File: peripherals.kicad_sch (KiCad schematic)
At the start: 50 parts, among them J5 Out_to_display, U1 Boost Converter - TPS61169DCKR, U3 RA8875L3N, U7 74HC4050D, Y1 20MHz

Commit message: Some fixes
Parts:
- removed C25, C26: 0.1uF, Capacitor_SMD:C_0805_2012Metric, symbol Device:C
- removed C27: 1uF, Capacitor_SMD:C_0805_2012Metric, symbol Device:C
- C31: value 0.1uF -> 1uF
- R38: value R -> 10k
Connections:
- net +3.3V: no longer C30.1, C31.1, C34.1
- net GND: now also C30.1; no longer C30.2
- net +1V5 renamed CORE_VDD
- net CORE_VDD: now also C30.2, C31.1; no longer U3.5 (OSC_VDD)
- new net: C34.1, U3.5 (OSC_VDD)
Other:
- moved on the sheet: C23, C24, C28, C29, C30, C31, C33, C34

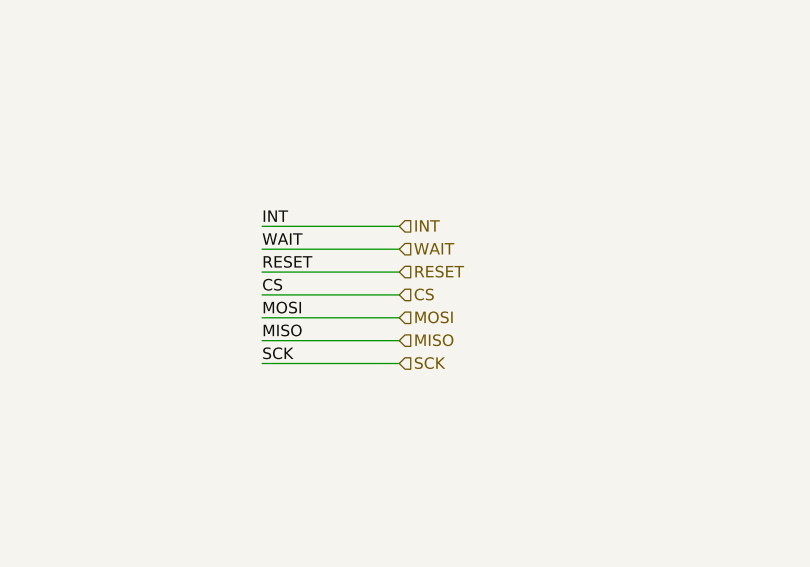
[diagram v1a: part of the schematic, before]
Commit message: Fixed labels and added datasheets
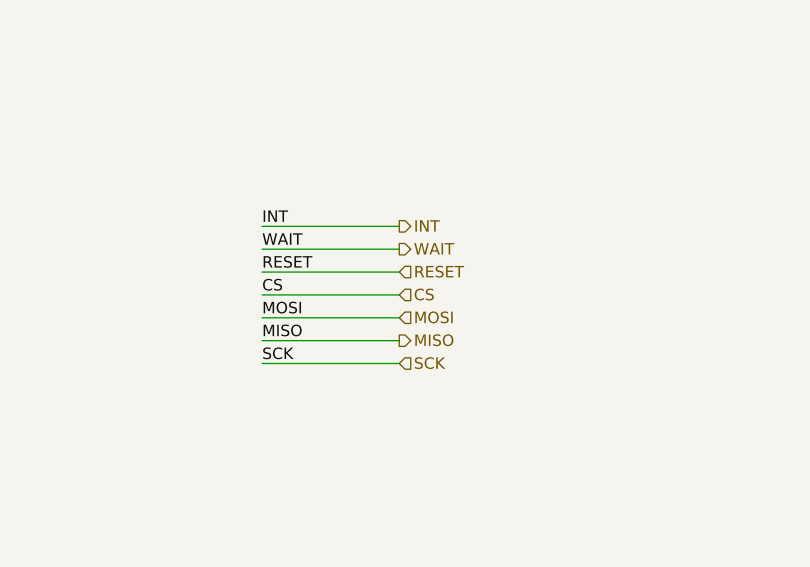
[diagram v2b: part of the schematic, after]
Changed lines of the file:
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@@
 	)
 	(hierarchical_label "INT"
-		(shape input)
+		(shape output)
 		(at 247.65 111.76 0)
 		(effects
@@
 	)
 	(hierarchical_label "MISO"
-		(shape input)
+		(shape output)
 		(at 247.65 124.46 0)
 		(effects
@@
 	)
 	(hierarchical_label "WAIT"
-		(shape input)
+		(shape output)
 		(at 247.65 114.3 0)
 		(effects
@@
 			)
 		)
-		(property "Datasheet" ""
+		(property "Datasheet" "https://assets.nexperia.com/documents/data-sheet/74HC4050.pdf"
 			(at 351.79 64.77 0)
 			(effects
@@
 			)
 		)
-		(property "Datasheet" ""
+		(property "Datasheet" "https://cdn-shop.adafruit.com/datasheets/RA8875_DS_V19_Eng.pdf"
 			(at 447.04 114.3 0)
 			(effects
@@
 			)
 		)
-		(property "Datasheet" ""
+		(property "Datasheet" "https://www.ti.com/lit/ds/symlink/tps61169.pdf"
 			(at 100.33 54.61 0)
 			(effects

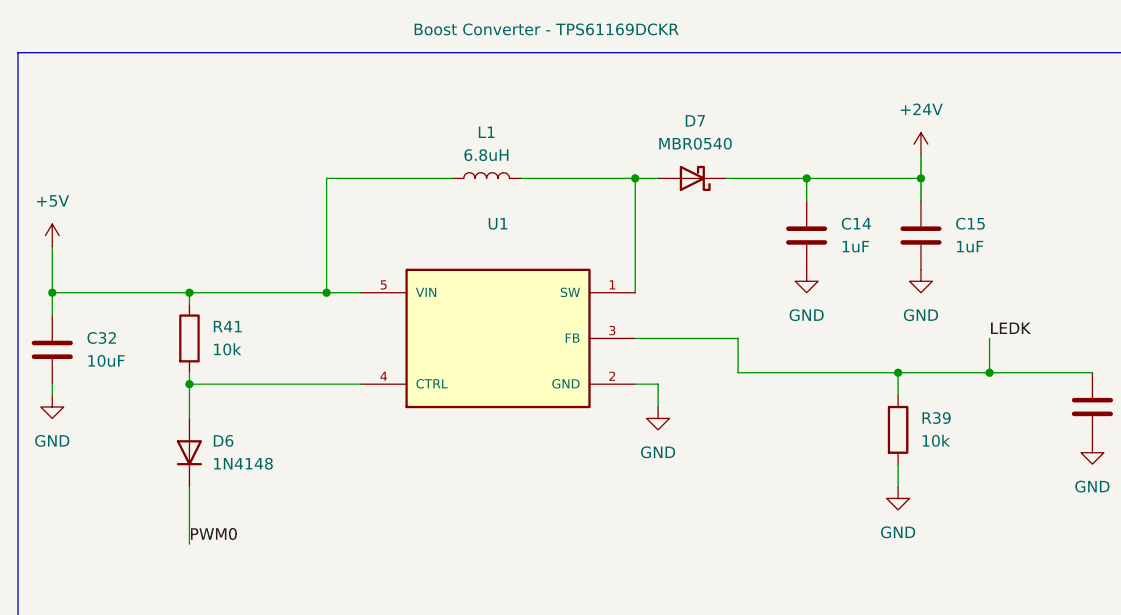
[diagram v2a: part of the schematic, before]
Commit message: boost converter
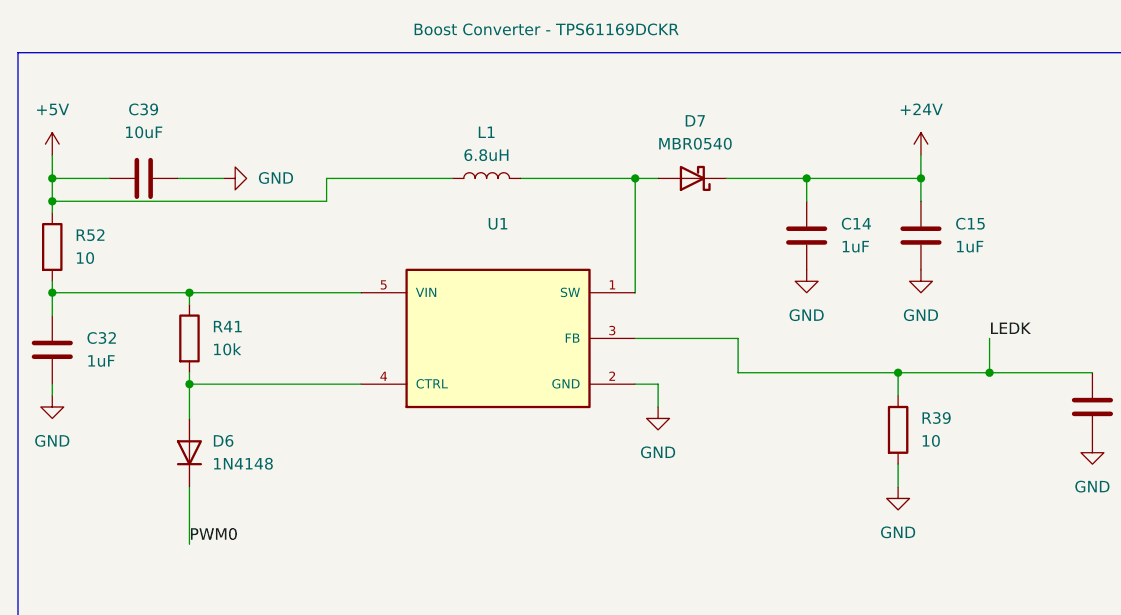
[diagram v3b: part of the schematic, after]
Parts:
- added C39: 10uF, Capacitor_SMD:C_0805_2012Metric, symbol Device:C
- added R52: 10, Resistor_SMD:R_0805_2012Metric_Pad1.20x1.40mm_HandSolder, symbol Device:R
- C32: value 10uF -> 1uF
- R39: value 10k -> 10
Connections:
- net +5V: now also C39.1, R52.1; no longer C32.1, R41.1, U1.5 (VIN)
- net GND: now also C39.2
- new net: C32.1, R41.1, R52.2, U1.5 (VIN)

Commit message: fixed several issues from review
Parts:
- C31: value 1uF -> .1uF
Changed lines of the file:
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@@
 			)
 		)
-		(property "Value" "1uF"
+		(property "Value" ".1uF"
 			(at 506.73 60.706 90)
 			(effects

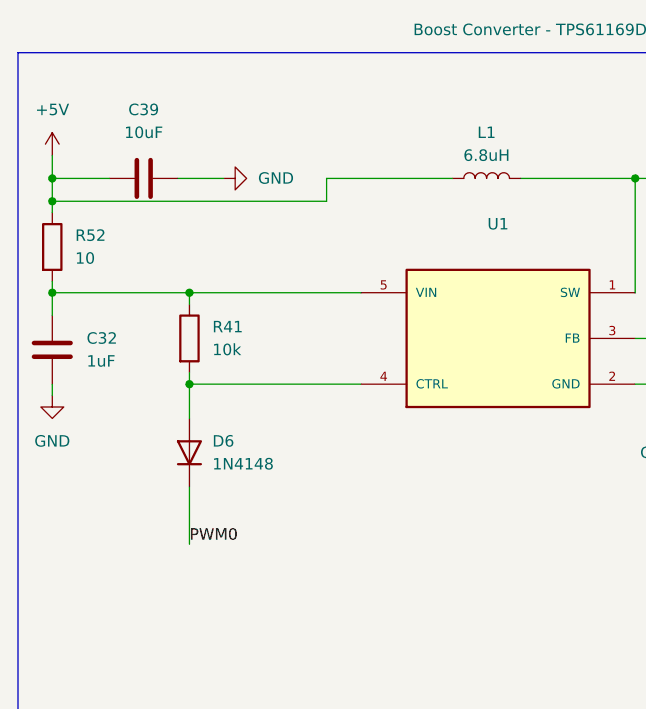
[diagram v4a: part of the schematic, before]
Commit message: u1 layout fix
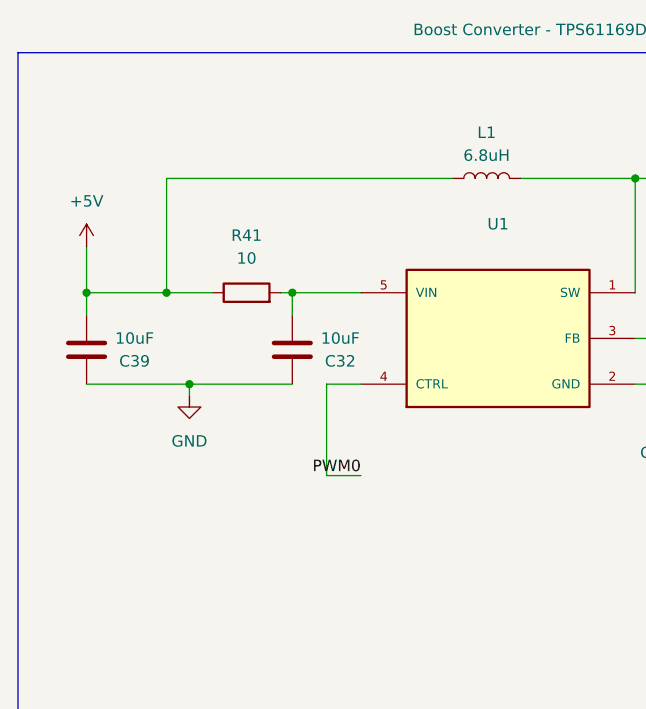
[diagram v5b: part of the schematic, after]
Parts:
- removed D6: 1N4148, Diode_THT:D_DO-35_SOD27_P7.62mm_Horizontal, symbol Diode:1N4148
- removed R52: 10, Resistor_SMD:R_0805_2012Metric_Pad1.20x1.40mm_HandSolder, symbol Device:R
- C32: value 1uF -> 10uF
- R41: value 10k -> 10
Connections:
- net +5V: now also C39.2, R41.1; no longer C39.1
- net GND: now also C32.1, C39.1; no longer C32.2, C39.2
- net PWM0: now also U1.4 (CTRL)
- net at R41.2: now also C32.2, U1.5 (VIN); no longer U1.4 (CTRL)
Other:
- moved on the sheet: C39, R41
